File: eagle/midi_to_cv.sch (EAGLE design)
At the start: 26 parts, among them U1 ATMEGA328P_PDIP

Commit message: noise and accent and raw gates
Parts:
- added C10: 47n, rcl:C-US025-040X050
- added C11: 2n7, rcl:C-US025-040X050
- added C12: 2n2, rcl:C-US025-040X050
- added C13: 1u/50v, rcl:CPOL-USB45181A
- added C8: 470pF, rcl:C-US025-040X050
- added C9: 18p, rcl:C-US025-040X050
- added D1, D3: (no value), SparkFun-DiscreteSemi:DIODE1N4148
- added JP1: (no value), adafruit:PINHD-2X4
- added OUTPUT: 22-23-2021, con-molex:22-23-2021
- added Q10, Q11, Q12, Q13, Q14, Q15, Q16, Q2, Q3, Q4, Q5, Q7, Q8, Q9: 2N3904, 808_lt:2N3904
- added Q6: 2SK30, 808:2SK30
- added R10: 1M5, rcl:R-US_0207/10
- added R11, R18, R20, R23, R25, R27, R29, R3, R31, R33, R35, R37: 15k, rcl:R-US_0207/10
- added R12: 47k, rcl:R-US_0207/10
- added R13: 100k, rcl:R-US_0207/10
- added R14: 2M2, rcl:R-US_0207/10
- added R16, R19, R21, R24, R26, R28, R30, R32, R34, R36, R38, R8, R9: 68k, rcl:R-US_0207/10
- added R17: 100k, pot:3RP/1610N
- added R7: 1M, rcl:R-US_0207/10
- added X1, X3: (no value), con-molex:22-23-2061
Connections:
- new net GND1: JP1.2, JP1.4, JP1.6, JP1.8, Q4.C, R10.2
- new net N$13: Q4.B, R10.1, R9.2
- new net N$14: Q7.C, R18.2
- new net N$15: C9.1, Q5.C, R11.2
- new net N$16: Q5.B, R12.2
- new net N$21: C9.2, D1.A, R13.1
- new net N$22: C10.1, D1.C, D3.C, R14.1
- new net N$23: D3.A, Q6.G
- new net N$24: C12.1, R16.1, R17.S, X1-1.S, X1-2.S, X1-3.S, X1-4.S, X1-5.S, X1-6.S, X3-1.S, X3-2.S, X3-3.S, X3-4.S, X3-5.S, X3-6.S
- new net N$25: Q7.B, R19.2
- new net N$26: C13.-, OUTPUT-2.S
- new net N$27: Q8.C, R20.2
- new net N$28: Q8.B, R21.2
- new net N$29: C11.1, C12.2, Q6.D, R17.E
- new net N$3: Q2.C, R3.2
- new net N$30: Q9.C, R23.2
- new net N$31: Q9.B, R24.2
- new net N$32: C11.2, C13.+, Q6.S, R16.2
- new net N$33: Q10.C, R25.2
- new net N$34: Q10.B, R26.2
- new net N$35: R21.1, U1.PC0(ADC0)
- new net N$36: Q11.C, R27.2
- new net N$37: Q11.B, R28.2
- new net N$38: Q12.C, R29.2
- new net N$39: Q12.B, R30.2
- new net N$40: Q13.C, R31.2
- new net N$41: Q13.B, R32.2
- new net N$42: Q14.C, R33.2
- new net N$43: Q14.B, R34.2
- new net N$44: Q15.C, R35.2
- new net N$45: Q15.B, R36.2
- new net N$46: Q16.C, R37.2
- new net N$47: Q16.B, R38.2
- new net N$48: R30.1, U1.PC1(ADC1)
- new net N$49: R36.1, U1.PC2(ADC2)
- new net N$50: R8.1, U1.PC3(ADC3)
- new net N$51: R19.1, U1.PC5(ADC5/SCL)
- new net N$52: R28.1, U1.PC4(ADC4/SDA)
- new net N$53: R34.1, U1.PD2(INT0)
- new net N$54: R26.1, U1.PD3(INT1)
- new net N$55: R24.1, U1.PD4(XCK/T0)
- new net N$56: R32.1, U1.PD5(T1)
- new net N$57: R38.1, U1.PD6(AIN0)
- new net N$6: C8.1, Q3.E, R7.2
- new net N$7: Q2.B, R8.2
- new net N$8: C8.2, R9.1
- net +12V: now also R11.1, R18.1, R20.1, R23.1, R25.1, R27.1, R29.1, R3.1, R31.1, R33.1, R35.1, R37.1, R7.1
- net GND: now also C10.2, JP1.1, JP1.3, JP1.5, JP1.7, OUTPUT-1.S, Q10.E, Q11.E, Q12.E, Q13.E, Q14.E, Q15.E, Q16.E, Q2.E, Q3.B, Q4.E, Q5.E, Q7.E, Q8.E, Q9.E, R13.2
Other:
- note added: "ACCENT"
- note added: "NOISE"

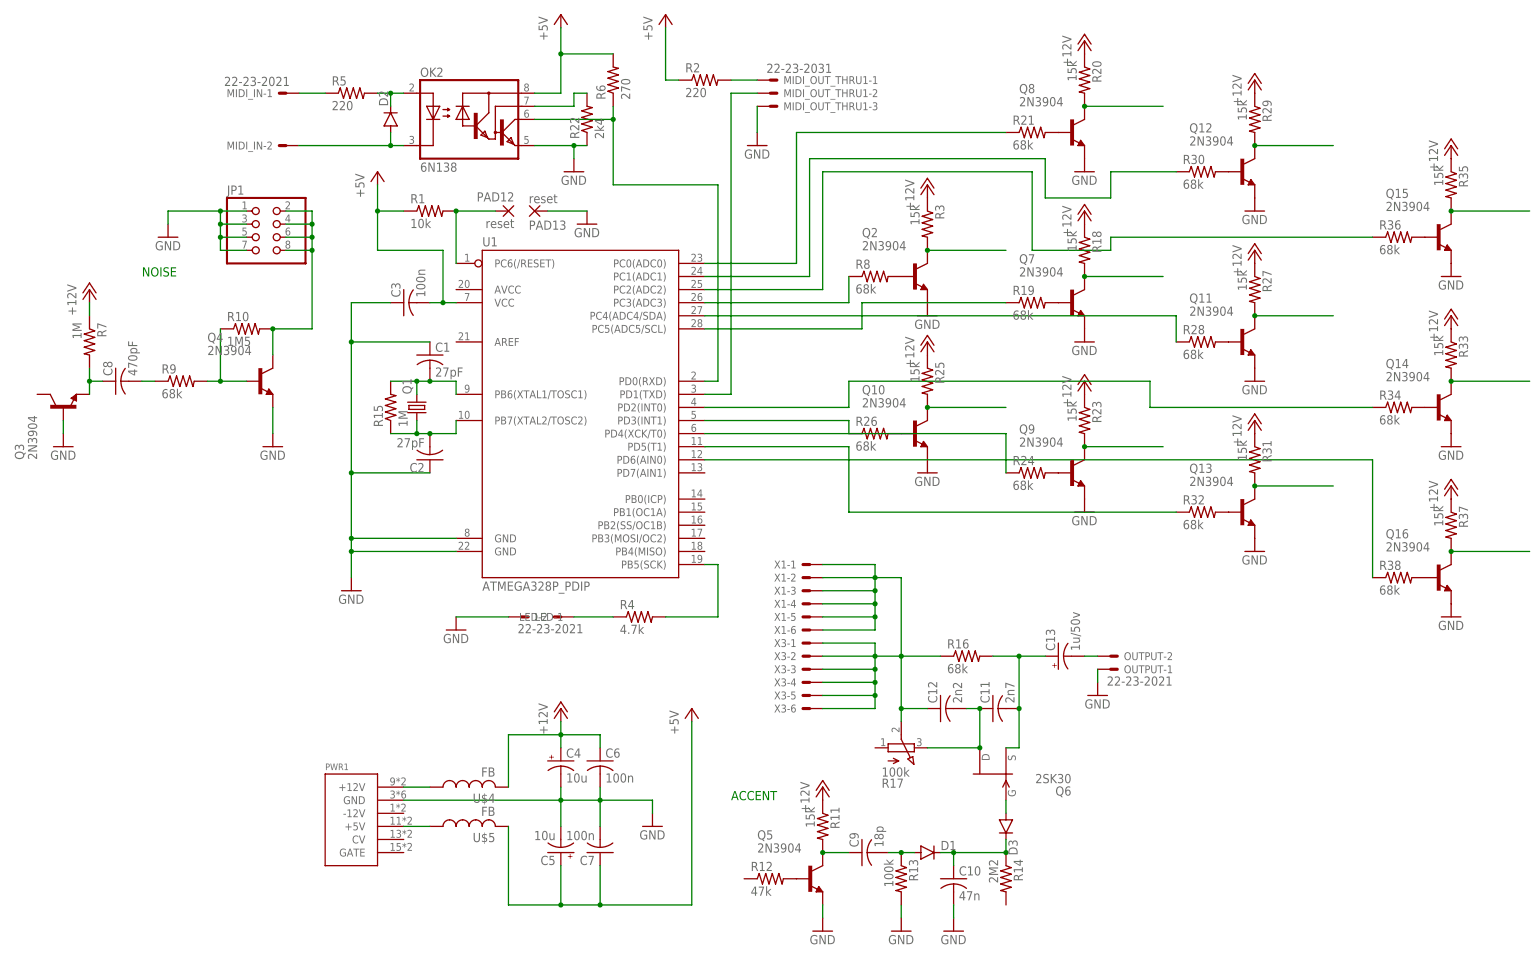
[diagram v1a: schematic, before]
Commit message: connectors for each voice
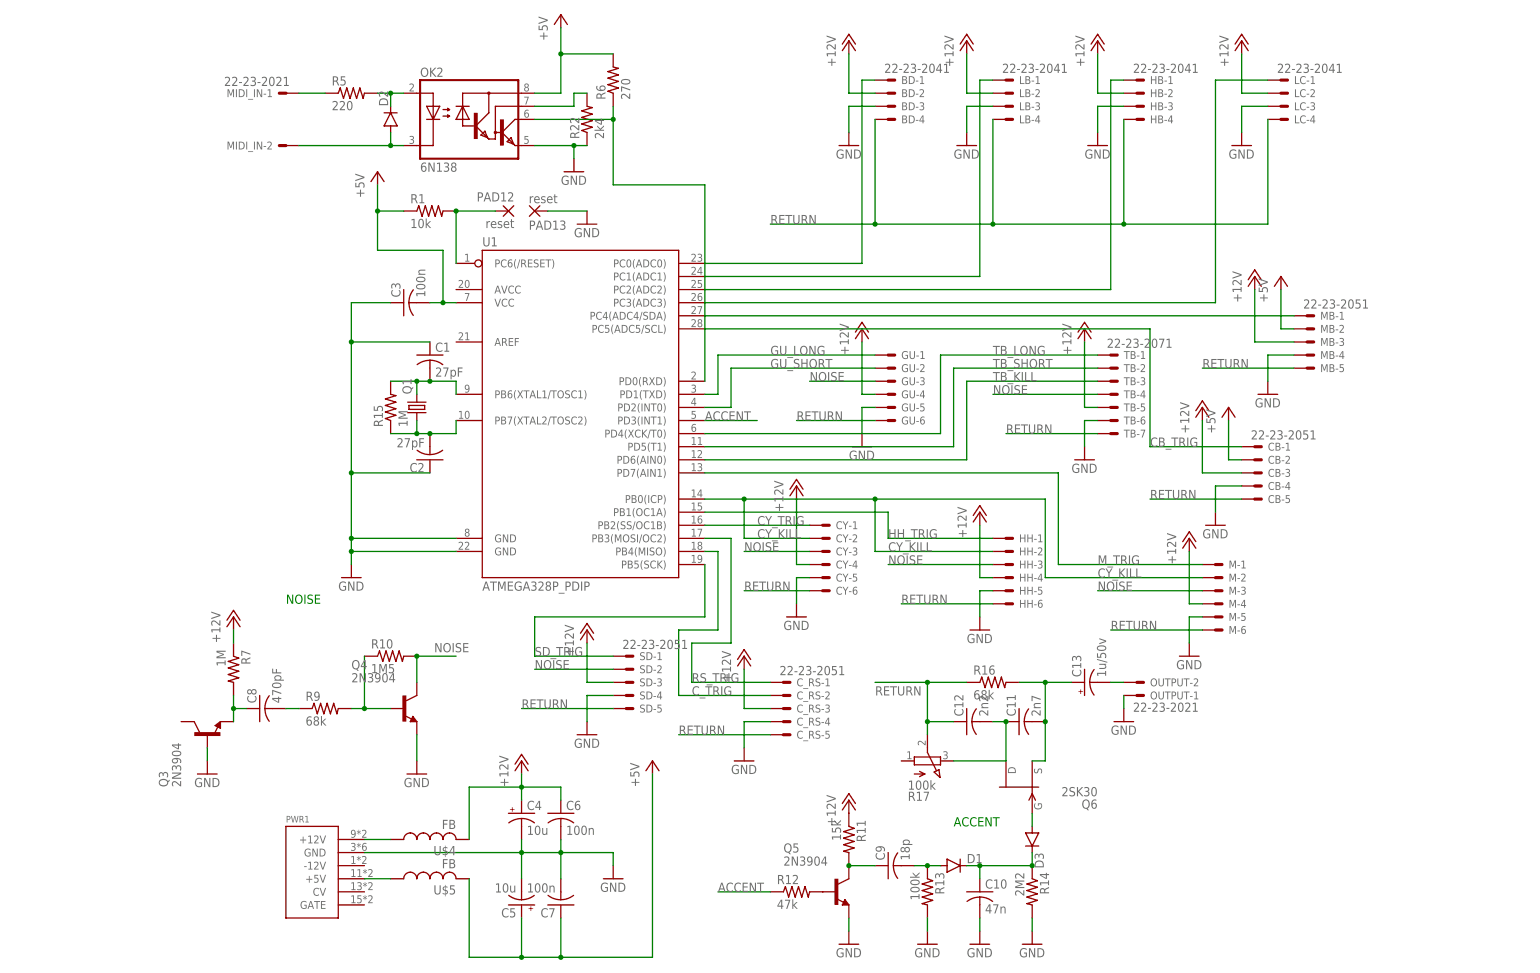
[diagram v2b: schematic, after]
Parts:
- removed JP1: (no value), adafruit:PINHD-2X4
- removed LED: 22-23-2021, con-molex:22-23-2021
- removed MIDI_OUT_THRU1: 22-23-2031, con-molex:22-23-2031
- removed Q10, Q11, Q12, Q13, Q14, Q15, Q16, Q2, Q7, Q8, Q9: 2N3904, 808_lt:2N3904
- removed R18, R20, R23, R25, R27, R29, R3, R31, R33, R35, R37: 15k, rcl:R-US_0207/10
- removed R19, R21, R24, R26, R28, R30, R32, R34, R36, R38, R8: 68k, rcl:R-US_0207/10
- removed R2: 220, rcl:R-US_0207/10
- removed R4: 4.7k, rcl:R-US_0207/10
- removed X1, X3: (no value), con-molex:22-23-2061
- added BD, HB, LB, LC: 22-23-2041, con-molex:22-23-2041
- added CB, C_RS, MB, SD: 22-23-2051, con-molex:22-23-2051
- added CY, GU, HH, M: (no value), con-molex:22-23-2061
- added TB: 22-23-2071, con-molex:22-23-2071
- R1, R10, R11, R13, R14, R16, R22, R6, R7, R9: device rcl:R-US_0207/10 -> rcl:R-US_0204/7
- R12: device rcl:R-US_0207/10 -> rcl:R-US_0207/12
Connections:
- removed net GND1: JP1.2, JP1.4, JP1.6, JP1.8, Q4.C, R10.2
- removed net N$10: R4.2, U1.PB5(SCK)
- removed net N$11: LED-2.S, R4.1
- removed net N$12: MIDI_OUT_THRU1-2.S, U1.PD1(TXD)
- removed net N$27: Q8.C, R20.2
- removed net N$28: Q8.B, R21.2
- removed net N$30: Q9.C, R23.2
- removed net N$31: Q9.B, R24.2
- removed net N$33: Q10.C, R25.2
- removed net N$34: Q10.B, R26.2
- removed net N$35: R21.1, U1.PC0(ADC0)
- removed net N$36: Q11.C, R27.2
- removed net N$37: Q11.B, R28.2
- removed net N$38: Q12.C, R29.2
- removed net N$39: Q12.B, R30.2
- removed net N$40: Q13.C, R31.2
- removed net N$41: Q13.B, R32.2
- removed net N$42: Q14.C, R33.2
- removed net N$43: Q14.B, R34.2
- removed net N$44: Q15.C, R35.2
- removed net N$45: Q15.B, R36.2
- removed net N$46: Q16.C, R37.2
- removed net N$47: Q16.B, R38.2
- removed net N$48: R30.1, U1.PC1(ADC1)
- removed net N$49: R36.1, U1.PC2(ADC2)
- removed net N$50: R8.1, U1.PC3(ADC3)
- removed net N$51: R19.1, U1.PC5(ADC5/SCL)
- removed net N$52: R28.1, U1.PC4(ADC4/SDA)
- removed net N$53: R34.1, U1.PD2(INT0)
- removed net N$54: R26.1, U1.PD3(INT1)
- removed net N$55: R24.1, U1.PD4(XCK/T0)
- removed net N$56: R32.1, U1.PD5(T1)
- removed net N$57: R38.1, U1.PD6(AIN0)
- removed net N$9: MIDI_OUT_THRU1-1.S, R2.2
- new net ACCENT: R12.1, U1.PD3(INT1)
- new net CB_TRIG: CB-1.S, U1.PC5(ADC5/SCL)
- new net CY_KILL: CY-2.S, HH-2.S, M-2.S, U1.PB0(ICP)
- new net CY_TRIG: CY-1.S, U1.PB2(SS/OC1B)
- new net C_TRIG: C_RS-2.S, U1.PB4(MISO)
- new net GU_LONG: GU-1.S, U1.PD1(TXD)
- new net GU_SHORT: GU-2.S, U1.PD2(INT0)
- new net HH_TRIG: HH-1.S, U1.PB1(OC1A)
- new net M_TRIG: M-1.S, U1.PD7(AIN1)
- new net NOISE: CY-3.S, GU-3.S, HH-3.S, M-3.S, Q4.C, R10.2, SD-2.S, TB-4.S
- new net RETURN: BD-4.S, C12.1, CB-5.S, CY-6.S, C_RS-5.S, GU-6.S, HB-4.S, HH-6.S, LB-4.S, LC-4.S, M-6.S, MB-5.S, R16.1, R17.S, SD-5.S, TB-7.S
- new net RS_TRIG: C_RS-1.S, U1.PB3(MOSI/OC2)
- new net SD_TRIG: SD-1.S, U1.PB5(SCK)
- new net TB_KILL: TB-3.S, U1.PD6(AIN0)
- new net TB_LONG: TB-1.S, U1.PD4(XCK/T0)
- new net TB_SHORT: TB-2.S, U1.PD5(T1)
- net +12V: now also BD-2.S, CB-3.S, CY-4.S, C_RS-3.S, GU-4.S, HB-2.S, HH-4.S, LB-2.S, LC-2.S, M-4.S, MB-3.S, SD-3.S, TB-5.S; no longer R18.1, R20.1, R23.1, R25.1, R27.1, R29.1, R3.1, R31.1, R33.1, R35.1, R37.1
- net +5V: now also CB-2.S, MB-2.S; no longer R2.1
- net GND: now also BD-3.S, CB-4.S, CY-5.S, C_RS-4.S, GU-5.S, HB-3.S, HH-5.S, LB-3.S, LC-3.S, M-5.S, MB-4.S, R14.2, SD-4.S, TB-6.S; no longer JP1.1, JP1.3, JP1.5, JP1.7, LED-1.S, MIDI_OUT_THRU1-3.S, Q10.E, Q11.E, Q12.E, Q13.E, Q14.E, Q15.E, Q16.E, Q2.E, Q7.E, Q8.E, Q9.E
- net N$14: now also HB-1.S, U1.PC2(ADC2); no longer Q7.C, R18.2
- net N$24: now also MB-1.S, U1.PC4(ADC4/SDA); no longer C12.1, R16.1, R17.S, X1-1.S, X1-2.S, X1-3.S, X1-4.S, X1-5.S, X1-6.S, X3-1.S, X3-2.S, X3-3.S, X3-4.S, X3-5.S, X3-6.S
- net N$25: now also LC-1.S, U1.PC3(ADC3); no longer Q7.B, R19.2
- net N$3: now also BD-1.S, U1.PC0(ADC0); no longer Q2.C, R3.2
- net N$7: now also LB-1.S, U1.PC1(ADC1); no longer Q2.B, R8.2
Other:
- moved on the sheet: C10, C11, C12, C13, C4, C5, C6, C7, C8, C9, D1, D3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

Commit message: 95pct auto
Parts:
- C9: device rcl:C-US025-040X050 -> rcl:C-US050-025X075
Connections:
- removed net GU_LONG: GU-1.S, U1.PD1(TXD)
- removed net GU_SHORT: GU-2.S, U1.PD2(INT0)
- new net N$10: GU-2.S, U1.PB5(SCK)
- new net N$9: GU-1.S, U1.PB4(MISO)
- net ACCENT: now also U1.PC5(ADC5/SCL); no longer U1.PD3(INT1)
- net CB_TRIG: now also U1.PD3(INT1); no longer U1.PC5(ADC5/SCL)
- net CY_KILL: now also U1.PD7(AIN1); no longer U1.PB0(ICP)
- net C_TRIG: now also U1.PC1(ADC1); no longer U1.PB4(MISO)
- net M_TRIG: now also U1.PB0(ICP); no longer U1.PD7(AIN1)
- net N$3: now also U1.PD1(TXD); no longer U1.PC0(ADC0)
- net N$7: now also U1.PD2(INT0); no longer U1.PC1(ADC1)
- net RS_TRIG: now also U1.PC0(ADC0); no longer U1.PB3(MOSI/OC2)
- net SD_TRIG: now also U1.PB3(MOSI/OC2); no longer U1.PB5(SCK)
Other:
- moved on the sheet: C_RS-1, C_RS-2, C_RS-3, C_RS-4, C_RS-5, GU-1, GU-2, GU-3, GU-4, GU-5, GU-6, R22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

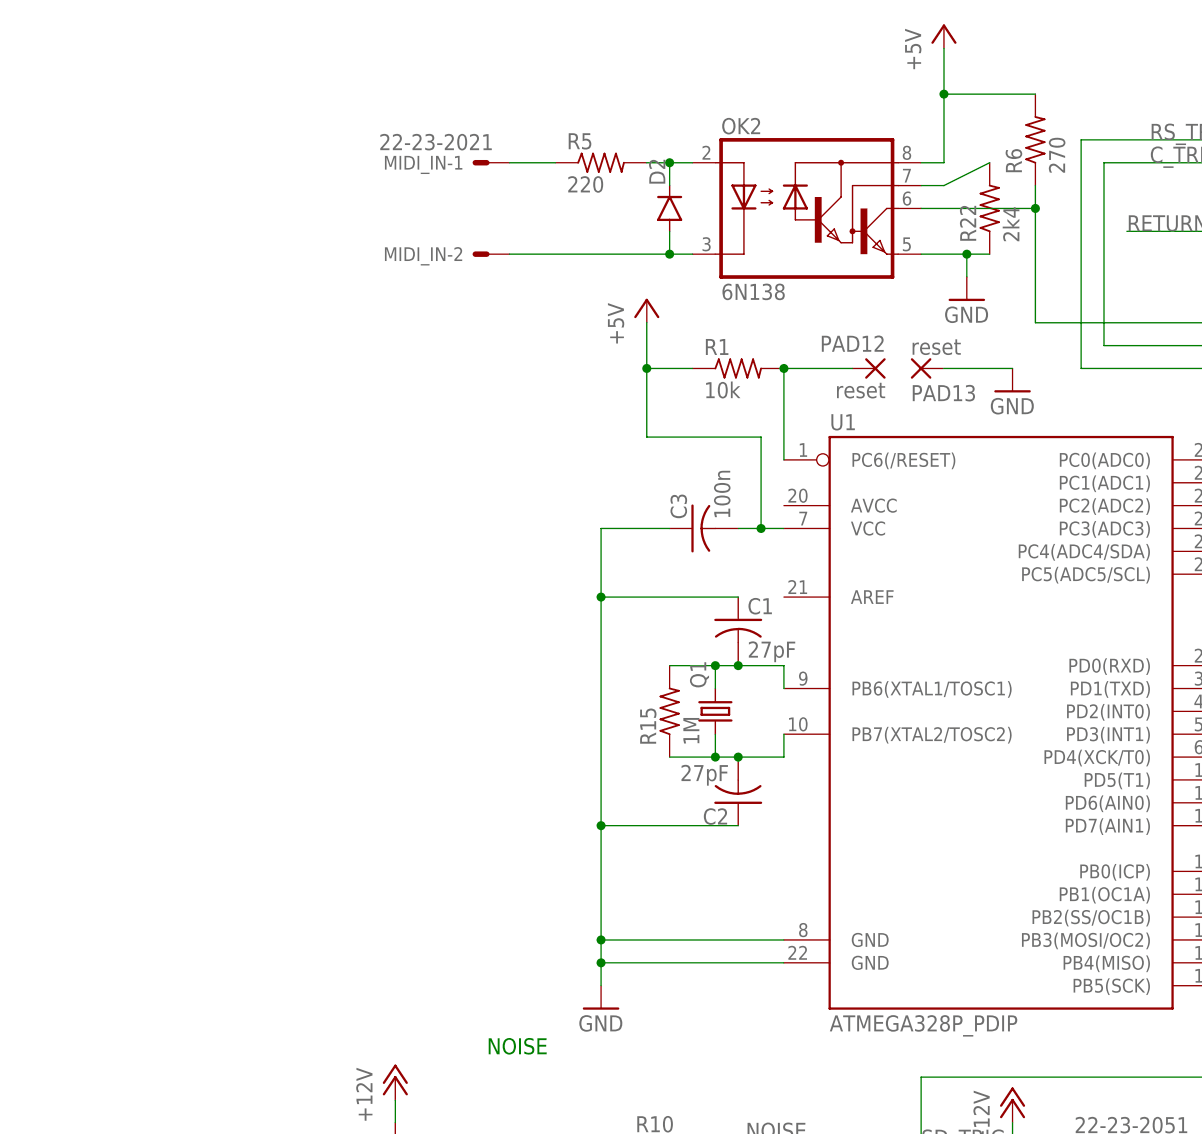
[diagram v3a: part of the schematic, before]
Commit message: added midi led and thru
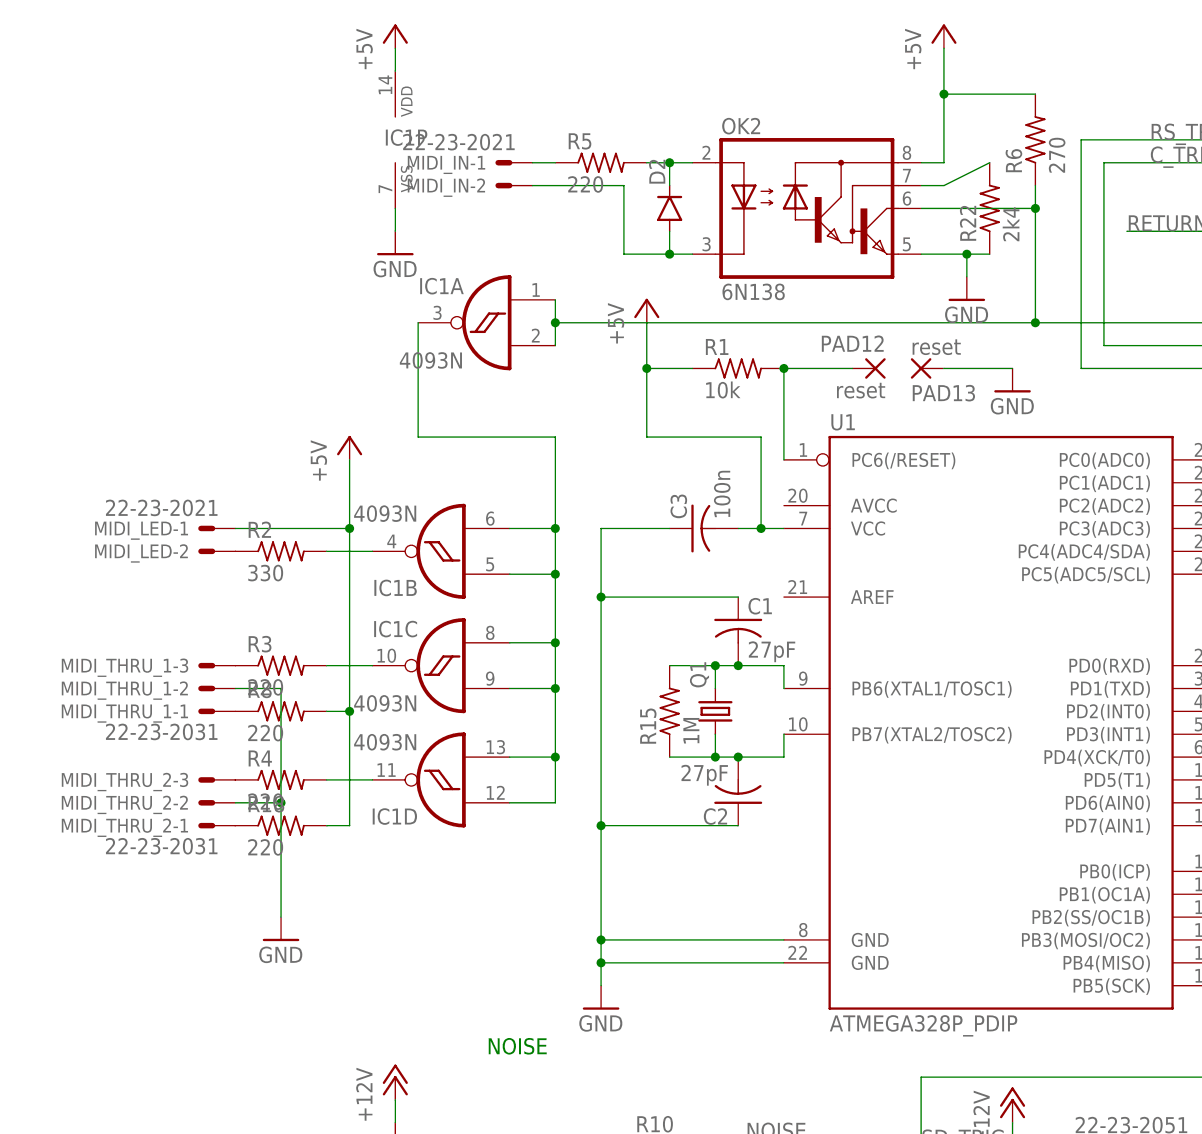
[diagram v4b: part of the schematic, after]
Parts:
- added IC1: 4093N, 40xx:4093N
- added MIDI_LED: 22-23-2021, con-molex:22-23-2021
- added MIDI_THRU_1, MIDI_THRU_2: 22-23-2031, con-molex:22-23-2031
- added R18, R3, R4, R8: 220, rcl:R-US_0204/7
- added R2: 330, rcl:R-US_0204/7
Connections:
- new net N$11: IC1A.I0, IC1A.I1, OK2.VO, R6.1, U1.PD0(RXD)
- new net N$12: IC1B.O, R2.2
- new net N$27: IC1C.O, R3.2
- new net N$28: IC1D.O, R4.2
- new net N$30: IC1A.O, IC1B.I0, IC1B.I1, IC1C.I0, IC1C.I1, IC1D.I0, IC1D.I1
- new net N$31: MIDI_LED-2.S, R2.1
- new net N$33: MIDI_THRU_1-3.S, R3.1
- new net N$34: MIDI_THRU_2-3.S, R4.1
- new net N$35: MIDI_THRU_2-1.S, R18.1
- net +5V: now also IC1P.VDD, MIDI_LED-1.S, R18.2, R8.2
- net GND: now also IC1P.VSS, MIDI_THRU_1-2.S, MIDI_THRU_2-2.S
- net N$20: now also MIDI_THRU_1-1.S, R8.1; no longer OK2.VO, R6.1, U1.PD0(RXD)
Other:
- moved on the sheet: MIDI_IN-1, MIDI_IN-2
